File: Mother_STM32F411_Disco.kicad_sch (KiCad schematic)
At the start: 34 parts, among them U1 ESP32-DEVKIT-V1

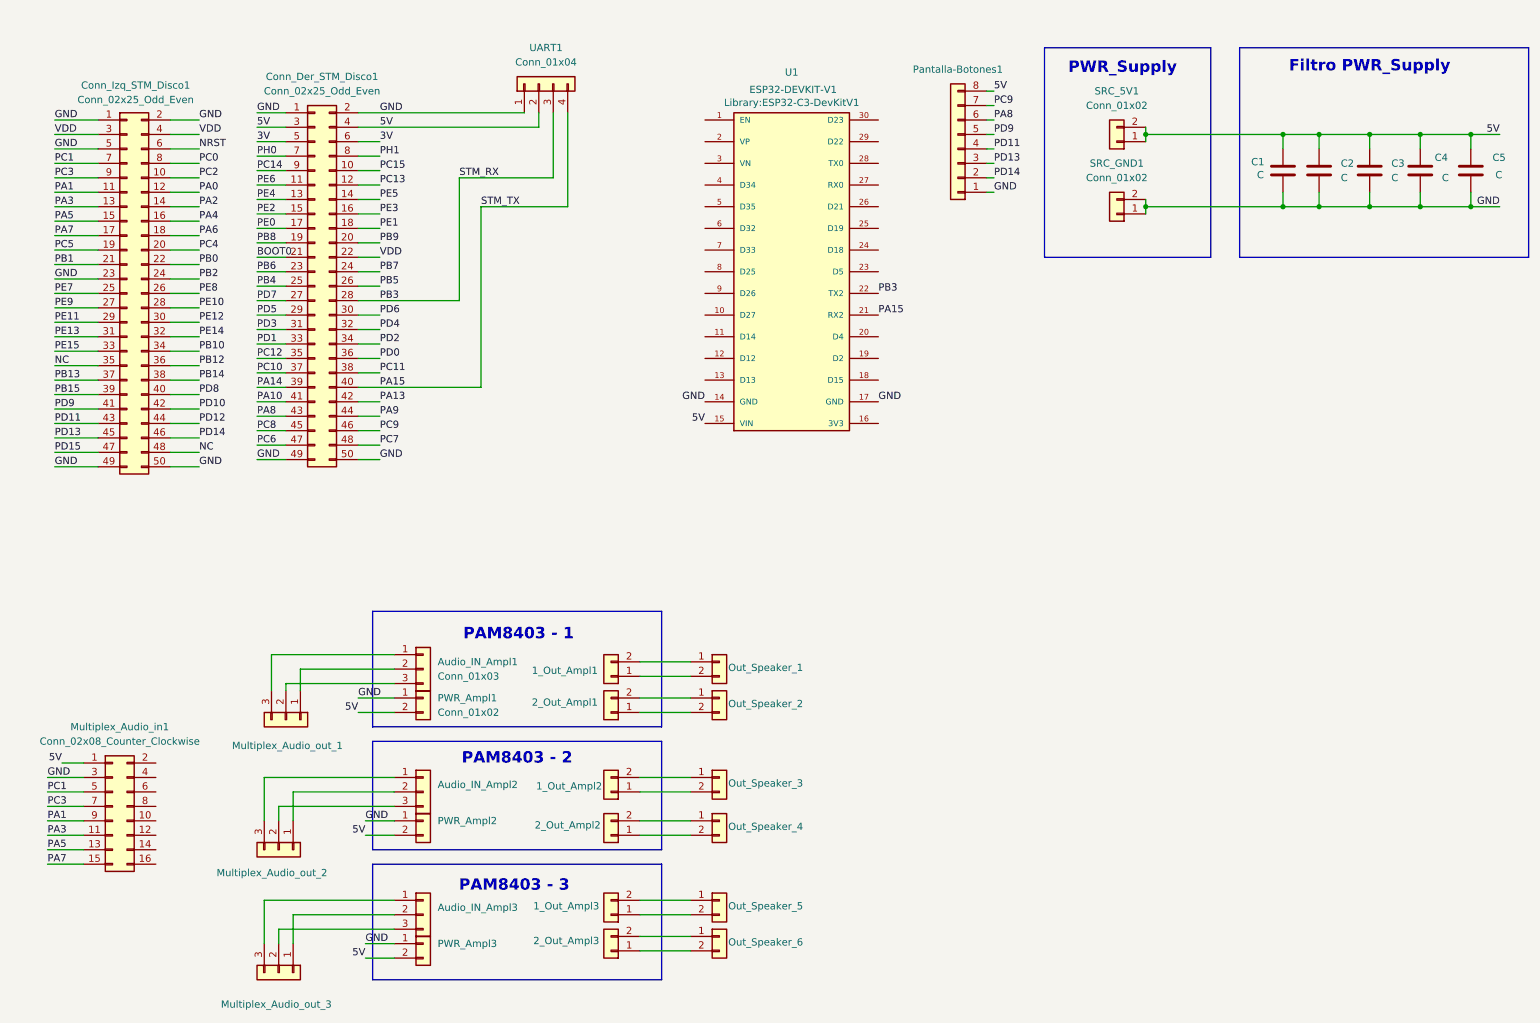
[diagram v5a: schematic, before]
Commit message: PCB layout preliminar
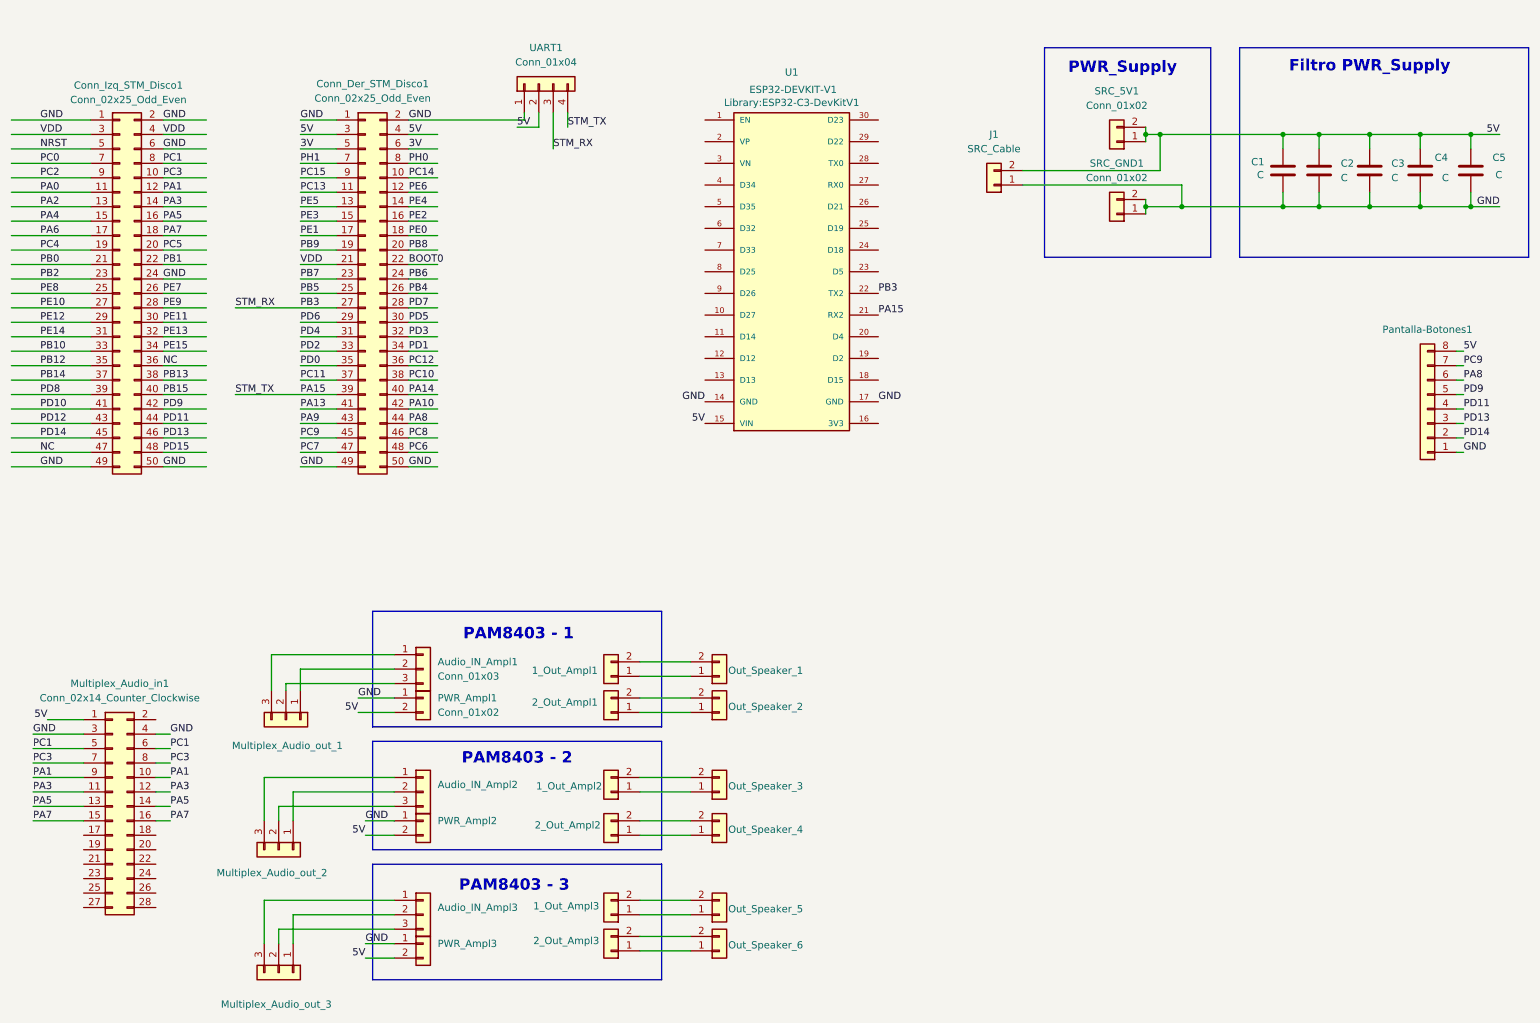
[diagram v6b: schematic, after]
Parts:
- added J1: SRC_Cable, TerminalBlock_Phoenix:TerminalBlock_Phoenix_MKDS-1,5-2_1x02_P5.00mm_Horizontal, symbol Connector_Generic:Conn_01x02
- Multiplex_Audio_in1: value Conn_02x08_Counter_Clockwise -> Conn_02x14_Counter_Clockwise; footprint Connector_PinHeader_2.54mm:PinHeader_2x08_P2.54mm_Vertical -> Connector_PinHeader_2.54mm:PinHeader_2x14_P2.54mm_Vertical; symbol Connector_Generic:Conn_02x08_Odd_Even -> Connector_Generic:Conn_02x14_Odd_Even
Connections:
- net 5V: now also J1.2 (Pin_2)
- net BOOT0: now also Conn_Der_STM_Disco1.22 (Pin_22); no longer Conn_Der_STM_Disco1.21 (Pin_21)
- net GND: now also Conn_Izq_STM_Disco1.24 (Pin_24), Conn_Izq_STM_Disco1.6 (Pin_6), Multiplex_Audio_in1.4 (Pin_4), J1.1 (Pin_1); no longer Conn_Izq_STM_Disco1.23 (Pin_23), Conn_Izq_STM_Disco1.5 (Pin_5)
- net NC: now also Conn_Izq_STM_Disco1.36 (Pin_36), Conn_Izq_STM_Disco1.47 (Pin_47); no longer Conn_Izq_STM_Disco1.35 (Pin_35), Conn_Izq_STM_Disco1.48 (Pin_48)
- net NRST: now also Conn_Izq_STM_Disco1.5 (Pin_5); no longer Conn_Izq_STM_Disco1.6 (Pin_6)
- net PA0: now also Conn_Izq_STM_Disco1.11 (Pin_11); no longer Conn_Izq_STM_Disco1.12 (Pin_12)
- net PA1: now also Conn_Izq_STM_Disco1.12 (Pin_12), Multiplex_Audio_in1.10 (Pin_10); no longer Conn_Izq_STM_Disco1.11 (Pin_11)
- net PA10: now also Conn_Der_STM_Disco1.42 (Pin_42); no longer Conn_Der_STM_Disco1.41 (Pin_41)
- net PA13: now also Conn_Der_STM_Disco1.41 (Pin_41); no longer Conn_Der_STM_Disco1.42 (Pin_42)
- net PA14: now also Conn_Der_STM_Disco1.40 (Pin_40); no longer Conn_Der_STM_Disco1.39 (Pin_39)
- net PA15: now also Conn_Der_STM_Disco1.39 (Pin_39); no longer Conn_Der_STM_Disco1.40 (Pin_40)
- net PA2: now also Conn_Izq_STM_Disco1.13 (Pin_13); no longer Conn_Izq_STM_Disco1.14 (Pin_14)
- net PA3: now also Conn_Izq_STM_Disco1.14 (Pin_14), Multiplex_Audio_in1.12 (Pin_12); no longer Conn_Izq_STM_Disco1.13 (Pin_13)
- net PA4: now also Conn_Izq_STM_Disco1.15 (Pin_15); no longer Conn_Izq_STM_Disco1.16 (Pin_16)
- net PA5: now also Conn_Izq_STM_Disco1.16 (Pin_16), Multiplex_Audio_in1.14 (Pin_14); no longer Conn_Izq_STM_Disco1.15 (Pin_15)
- net PA6: now also Conn_Izq_STM_Disco1.17 (Pin_17); no longer Conn_Izq_STM_Disco1.18 (Pin_18)
- net PA7: now also Conn_Izq_STM_Disco1.18 (Pin_18), Multiplex_Audio_in1.16 (Pin_16); no longer Conn_Izq_STM_Disco1.17 (Pin_17)
- net PA8: now also Conn_Der_STM_Disco1.44 (Pin_44); no longer Conn_Der_STM_Disco1.43 (Pin_43)
- net PA9: now also Conn_Der_STM_Disco1.43 (Pin_43); no longer Conn_Der_STM_Disco1.44 (Pin_44)
- net PB0: now also Conn_Izq_STM_Disco1.21 (Pin_21); no longer Conn_Izq_STM_Disco1.22 (Pin_22)
- net PB1: now also Conn_Izq_STM_Disco1.22 (Pin_22); no longer Conn_Izq_STM_Disco1.21 (Pin_21)
- net PB10: now also Conn_Izq_STM_Disco1.33 (Pin_33); no longer Conn_Izq_STM_Disco1.34 (Pin_34)
- net PB12: now also Conn_Izq_STM_Disco1.35 (Pin_35); no longer Conn_Izq_STM_Disco1.36 (Pin_36)
- net PB13: now also Conn_Izq_STM_Disco1.38 (Pin_38); no longer Conn_Izq_STM_Disco1.37 (Pin_37)
- net PB14: now also Conn_Izq_STM_Disco1.37 (Pin_37); no longer Conn_Izq_STM_Disco1.38 (Pin_38)
- net PB15: now also Conn_Izq_STM_Disco1.40 (Pin_40); no longer Conn_Izq_STM_Disco1.39 (Pin_39)
- net PB2: now also Conn_Izq_STM_Disco1.23 (Pin_23); no longer Conn_Izq_STM_Disco1.24 (Pin_24)
- net PB3: now also Conn_Der_STM_Disco1.27 (Pin_27); no longer Conn_Der_STM_Disco1.28 (Pin_28)
- net PB4: now also Conn_Der_STM_Disco1.26 (Pin_26); no longer Conn_Der_STM_Disco1.25 (Pin_25)
- net PB5: now also Conn_Der_STM_Disco1.25 (Pin_25); no longer Conn_Der_STM_Disco1.26 (Pin_26)
- net PB6: now also Conn_Der_STM_Disco1.24 (Pin_24); no longer Conn_Der_STM_Disco1.23 (Pin_23)
- net PB7: now also Conn_Der_STM_Disco1.23 (Pin_23); no longer Conn_Der_STM_Disco1.24 (Pin_24)
- net PB8: now also Conn_Der_STM_Disco1.20 (Pin_20); no longer Conn_Der_STM_Disco1.19 (Pin_19)
- net PB9: now also Conn_Der_STM_Disco1.19 (Pin_19); no longer Conn_Der_STM_Disco1.20 (Pin_20)
- net PC0: now also Conn_Izq_STM_Disco1.7 (Pin_7); no longer Conn_Izq_STM_Disco1.8 (Pin_8)
- net PC1: now also Conn_Izq_STM_Disco1.8 (Pin_8), Multiplex_Audio_in1.6 (Pin_6); no longer Conn_Izq_STM_Disco1.7 (Pin_7)
- net PC10: now also Conn_Der_STM_Disco1.38 (Pin_38); no longer Conn_Der_STM_Disco1.37 (Pin_37)
- net PC11: now also Conn_Der_STM_Disco1.37 (Pin_37); no longer Conn_Der_STM_Disco1.38 (Pin_38)
- net PC12: now also Conn_Der_STM_Disco1.36 (Pin_36); no longer Conn_Der_STM_Disco1.35 (Pin_35)
- net PC13: now also Conn_Der_STM_Disco1.11 (Pin_11); no longer Conn_Der_STM_Disco1.12 (Pin_12)
- net PC14: now also Conn_Der_STM_Disco1.10 (Pin_10); no longer Conn_Der_STM_Disco1.9 (Pin_9)
- net PC15: now also Conn_Der_STM_Disco1.9 (Pin_9); no longer Conn_Der_STM_Disco1.10 (Pin_10)
- net PC2: now also Conn_Izq_STM_Disco1.9 (Pin_9); no longer Conn_Izq_STM_Disco1.10 (Pin_10)
- net PC3: now also Conn_Izq_STM_Disco1.10 (Pin_10), Multiplex_Audio_in1.8 (Pin_8); no longer Conn_Izq_STM_Disco1.9 (Pin_9)
- net PC4: now also Conn_Izq_STM_Disco1.19 (Pin_19); no longer Conn_Izq_STM_Disco1.20 (Pin_20)
- net PC5: now also Conn_Izq_STM_Disco1.20 (Pin_20); no longer Conn_Izq_STM_Disco1.19 (Pin_19)
- net PC6: now also Conn_Der_STM_Disco1.48 (Pin_48); no longer Conn_Der_STM_Disco1.47 (Pin_47)
- net PC7: now also Conn_Der_STM_Disco1.47 (Pin_47); no longer Conn_Der_STM_Disco1.48 (Pin_48)
- net PC8: now also Conn_Der_STM_Disco1.46 (Pin_46); no longer Conn_Der_STM_Disco1.45 (Pin_45)
- net PC9: now also Conn_Der_STM_Disco1.45 (Pin_45); no longer Conn_Der_STM_Disco1.46 (Pin_46)
- net PD0: now also Conn_Der_STM_Disco1.35 (Pin_35); no longer Conn_Der_STM_Disco1.36 (Pin_36)
- net PD1: now also Conn_Der_STM_Disco1.34 (Pin_34); no longer Conn_Der_STM_Disco1.33 (Pin_33)
- net PD10: now also Conn_Izq_STM_Disco1.41 (Pin_41); no longer Conn_Izq_STM_Disco1.42 (Pin_42)
- net PD11: now also Conn_Izq_STM_Disco1.44 (Pin_44); no longer Conn_Izq_STM_Disco1.43 (Pin_43)
- net PD12: now also Conn_Izq_STM_Disco1.43 (Pin_43); no longer Conn_Izq_STM_Disco1.44 (Pin_44)
- net PD13: now also Conn_Izq_STM_Disco1.46 (Pin_46); no longer Conn_Izq_STM_Disco1.45 (Pin_45)
- net PD14: now also Conn_Izq_STM_Disco1.45 (Pin_45); no longer Conn_Izq_STM_Disco1.46 (Pin_46)
- net PD15: now also Conn_Izq_STM_Disco1.48 (Pin_48); no longer Conn_Izq_STM_Disco1.47 (Pin_47)
- net PD2: now also Conn_Der_STM_Disco1.33 (Pin_33); no longer Conn_Der_STM_Disco1.34 (Pin_34)
- net PD3: now also Conn_Der_STM_Disco1.32 (Pin_32); no longer Conn_Der_STM_Disco1.31 (Pin_31)
- net PD4: now also Conn_Der_STM_Disco1.31 (Pin_31); no longer Conn_Der_STM_Disco1.32 (Pin_32)
- net PD5: now also Conn_Der_STM_Disco1.30 (Pin_30); no longer Conn_Der_STM_Disco1.29 (Pin_29)
- net PD6: now also Conn_Der_STM_Disco1.29 (Pin_29); no longer Conn_Der_STM_Disco1.30 (Pin_30)
- net PD7: now also Conn_Der_STM_Disco1.28 (Pin_28); no longer Conn_Der_STM_Disco1.27 (Pin_27)
- net PD8: now also Conn_Izq_STM_Disco1.39 (Pin_39); no longer Conn_Izq_STM_Disco1.40 (Pin_40)
- net PD9: now also Conn_Izq_STM_Disco1.42 (Pin_42); no longer Conn_Izq_STM_Disco1.41 (Pin_41)
- net PE0: now also Conn_Der_STM_Disco1.18 (Pin_18); no longer Conn_Der_STM_Disco1.17 (Pin_17)
- net PE1: now also Conn_Der_STM_Disco1.17 (Pin_17); no longer Conn_Der_STM_Disco1.18 (Pin_18)
- net PE10: now also Conn_Izq_STM_Disco1.27 (Pin_27); no longer Conn_Izq_STM_Disco1.28 (Pin_28)
- net PE11: now also Conn_Izq_STM_Disco1.30 (Pin_30); no longer Conn_Izq_STM_Disco1.29 (Pin_29)
- net PE12: now also Conn_Izq_STM_Disco1.29 (Pin_29); no longer Conn_Izq_STM_Disco1.30 (Pin_30)
- net PE13: now also Conn_Izq_STM_Disco1.32 (Pin_32); no longer Conn_Izq_STM_Disco1.31 (Pin_31)
- net PE14: now also Conn_Izq_STM_Disco1.31 (Pin_31); no longer Conn_Izq_STM_Disco1.32 (Pin_32)
- net PE15: now also Conn_Izq_STM_Disco1.34 (Pin_34); no longer Conn_Izq_STM_Disco1.33 (Pin_33)
- net PE2: now also Conn_Der_STM_Disco1.16 (Pin_16); no longer Conn_Der_STM_Disco1.15 (Pin_15)
- net PE3: now also Conn_Der_STM_Disco1.15 (Pin_15); no longer Conn_Der_STM_Disco1.16 (Pin_16)
- net PE4: now also Conn_Der_STM_Disco1.14 (Pin_14); no longer Conn_Der_STM_Disco1.13 (Pin_13)
- net PE5: now also Conn_Der_STM_Disco1.13 (Pin_13); no longer Conn_Der_STM_Disco1.14 (Pin_14)
- net PE6: now also Conn_Der_STM_Disco1.12 (Pin_12); no longer Conn_Der_STM_Disco1.11 (Pin_11)
- net PE7: now also Conn_Izq_STM_Disco1.26 (Pin_26); no longer Conn_Izq_STM_Disco1.25 (Pin_25)
- net PE8: now also Conn_Izq_STM_Disco1.25 (Pin_25); no longer Conn_Izq_STM_Disco1.26 (Pin_26)
- net PE9: now also Conn_Izq_STM_Disco1.28 (Pin_28); no longer Conn_Izq_STM_Disco1.27 (Pin_27)
- net PH0: now also Conn_Der_STM_Disco1.8 (Pin_8); no longer Conn_Der_STM_Disco1.7 (Pin_7)
- net PH1: now also Conn_Der_STM_Disco1.7 (Pin_7); no longer Conn_Der_STM_Disco1.8 (Pin_8)
- net VDD: now also Conn_Der_STM_Disco1.21 (Pin_21); no longer Conn_Der_STM_Disco1.22 (Pin_22)
- net at 2_Out_Ampl2.1 (Pin_1): now also Out_Speaker_4.1 (Pin_1); no longer Out_Speaker_4.2 (Pin_2)
- net at 2_Out_Ampl2.2 (Pin_2): now also Out_Speaker_4.2 (Pin_2); no longer Out_Speaker_4.1 (Pin_1)
- net at 1_Out_Ampl2.1 (Pin_1): now also Out_Speaker_3.1 (Pin_1); no longer Out_Speaker_3.2 (Pin_2)
- net at 1_Out_Ampl2.2 (Pin_2): now also Out_Speaker_3.2 (Pin_2); no longer Out_Speaker_3.1 (Pin_1)
- net at 1_Out_Ampl1.1 (Pin_1): now also Out_Speaker_1.1 (Pin_1); no longer Out_Speaker_1.2 (Pin_2)
- net at 1_Out_Ampl1.2 (Pin_2): now also Out_Speaker_1.2 (Pin_2); no longer Out_Speaker_1.1 (Pin_1)
- net at 2_Out_Ampl1.1 (Pin_1): now also Out_Speaker_2.1 (Pin_1); no longer Out_Speaker_2.2 (Pin_2)
- net at 2_Out_Ampl1.2 (Pin_2): now also Out_Speaker_2.2 (Pin_2); no longer Out_Speaker_2.1 (Pin_1)
- net at Out_Speaker_6.1 (Pin_1): now also 2_Out_Ampl3.1 (Pin_1); no longer 2_Out_Ampl3.2 (Pin_2)
- net at Out_Speaker_6.2 (Pin_2): now also 2_Out_Ampl3.2 (Pin_2); no longer 2_Out_Ampl3.1 (Pin_1)
- net at Out_Speaker_5.1 (Pin_1): now also 1_Out_Ampl3.1 (Pin_1); no longer 1_Out_Ampl3.2 (Pin_2)
- net at Out_Speaker_5.2 (Pin_2): now also 1_Out_Ampl3.2 (Pin_2); no longer 1_Out_Ampl3.1 (Pin_1)
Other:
- moved on the sheet: Conn_Der_STM_Disco1, Conn_Izq_STM_Disco1, Pantalla-Botones1

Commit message: Huellas OK, PCB layout OK
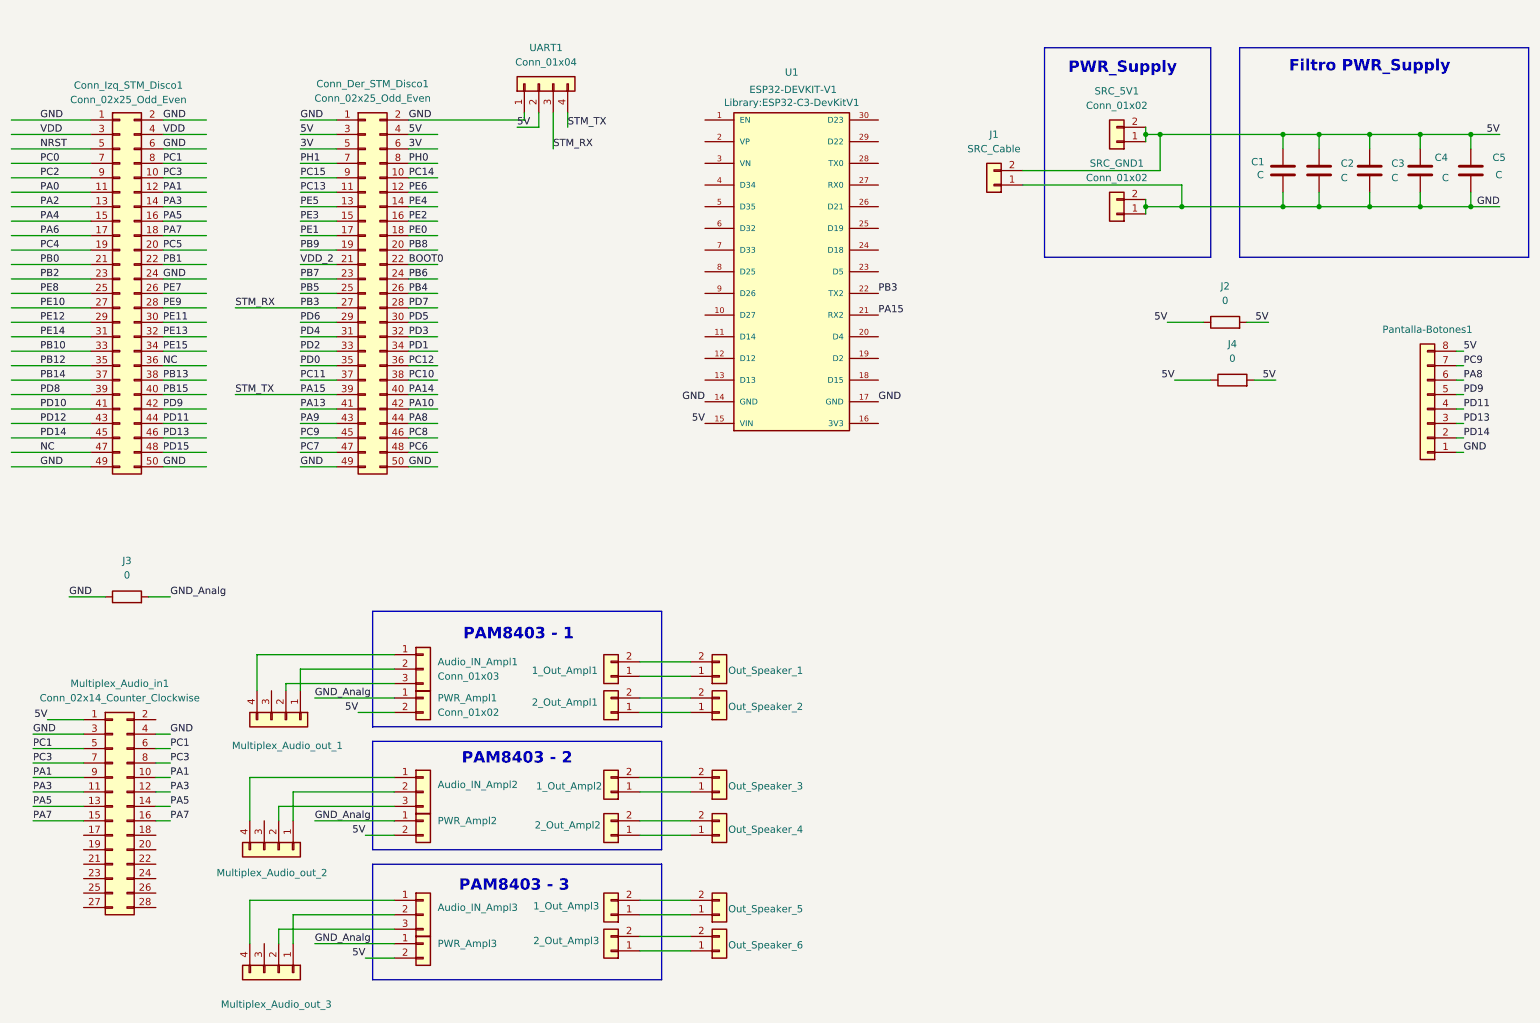
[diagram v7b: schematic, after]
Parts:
- added J2, J3, J4: 0, Resistor_SMD:R_1210_3225Metric_Pad1.30x2.65mm_HandSolder, symbol Device:R
- Multiplex_Audio_out_1, Multiplex_Audio_out_2, Multiplex_Audio_out_3: value Conn_01x03 -> Conn_01x04; footprint Connector_PinSocket_2.54mm:PinSocket_1x03_P2.54mm_Vertical -> Connector_PinSocket_2.54mm:PinSocket_1x04_P2.54mm_Vertical; symbol Connector_Generic:Conn_01x03 -> Connector_Generic:Conn_01x04
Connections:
- net 5V: now also J2.1, J2.2, J4.1, J4.2
- net GND: now also J3.1; no longer PWR_Ampl1.1 (Pin_1), PWR_Ampl2.1 (Pin_1), PWR_Ampl3.1 (Pin_1)
- net VDD: no longer Conn_Der_STM_Disco1.21 (Pin_21)
- net at Multiplex_Audio_out_3.3 (Pin_3): no longer Audio_IN_Ampl3.1 (Pin_1)
- net at Multiplex_Audio_out_2.3 (Pin_3): no longer Audio_IN_Ampl2.1 (Pin_1)
- net at Multiplex_Audio_out_1.3 (Pin_3): no longer Audio_IN_Ampl1.1 (Pin_1)
- new net: Audio_IN_Ampl3.1 (Pin_1), Multiplex_Audio_out_3.4 (Pin_4)
- new net: Audio_IN_Ampl2.1 (Pin_1), Multiplex_Audio_out_2.4 (Pin_4)
- new net: Audio_IN_Ampl1.1 (Pin_1), Multiplex_Audio_out_1.4 (Pin_4)
- new net GND_Analg: J3.2, PWR_Ampl1.1 (Pin_1), PWR_Ampl2.1 (Pin_1), PWR_Ampl3.1 (Pin_1)
- new net VDD_2: Conn_Der_STM_Disco1.21 (Pin_21)

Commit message: PCB version 2
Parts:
- added J5, J6: 0, Resistor_SMD:R_1210_3225Metric_Pad1.30x2.65mm_HandSolder, symbol Device:R
- Pantalla-Botones1: footprint Connector_PinSocket_2.54mm:PinSocket_1x08_P2.54mm_Vertical -> Connector_PinHeader_2.54mm:PinHeader_1x08_P2.54mm_Horizontal
- UART1: footprint Connector_PinHeader_2.54mm:PinHeader_1x04_P2.54mm_Horizontal -> Connector_PinHeader_2.54mm:PinHeader_1x05_P2.54mm_Horizontal; symbol Connector_Generic:Conn_01x04 -> Connector_Generic:Conn_01x05
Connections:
- net 5V: now also Pantalla-Botones1.1 (Pin_1), J6.1; no longer Pantalla-Botones1.8 (Pin_8), UART1.2 (Pin_2)
- net GND: now also Pantalla-Botones1.8 (Pin_8), J5.1; no longer Pantalla-Botones1.1 (Pin_1), UART1.1 (Pin_1)
- net PA15: now also UART1.3 (Pin_3); no longer UART1.4 (Pin_4)
- net PA8: now also Pantalla-Botones1.3 (Pin_3); no longer Pantalla-Botones1.6 (Pin_6)
- net PB3: now also UART1.4 (Pin_4); no longer UART1.3 (Pin_3)
- net PC9: now also Pantalla-Botones1.2 (Pin_2); no longer Pantalla-Botones1.7 (Pin_7)
- net PD11: now also Pantalla-Botones1.5 (Pin_5); no longer Pantalla-Botones1.4 (Pin_4)
- net PD13: now also Pantalla-Botones1.6 (Pin_6); no longer Pantalla-Botones1.3 (Pin_3)
- net PD14: now also Pantalla-Botones1.7 (Pin_7); no longer Pantalla-Botones1.2 (Pin_2)
- net PD9: now also Pantalla-Botones1.4 (Pin_4); no longer Pantalla-Botones1.5 (Pin_5)
- new net: J5.2, UART1.2 (Pin_2)
- new net: J6.2, UART1.1 (Pin_1)
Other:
- moved on the sheet: Pantalla-Botones1
